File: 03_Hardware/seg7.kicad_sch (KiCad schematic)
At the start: 49 parts, among them Q201 BC807, U201 SMA41056

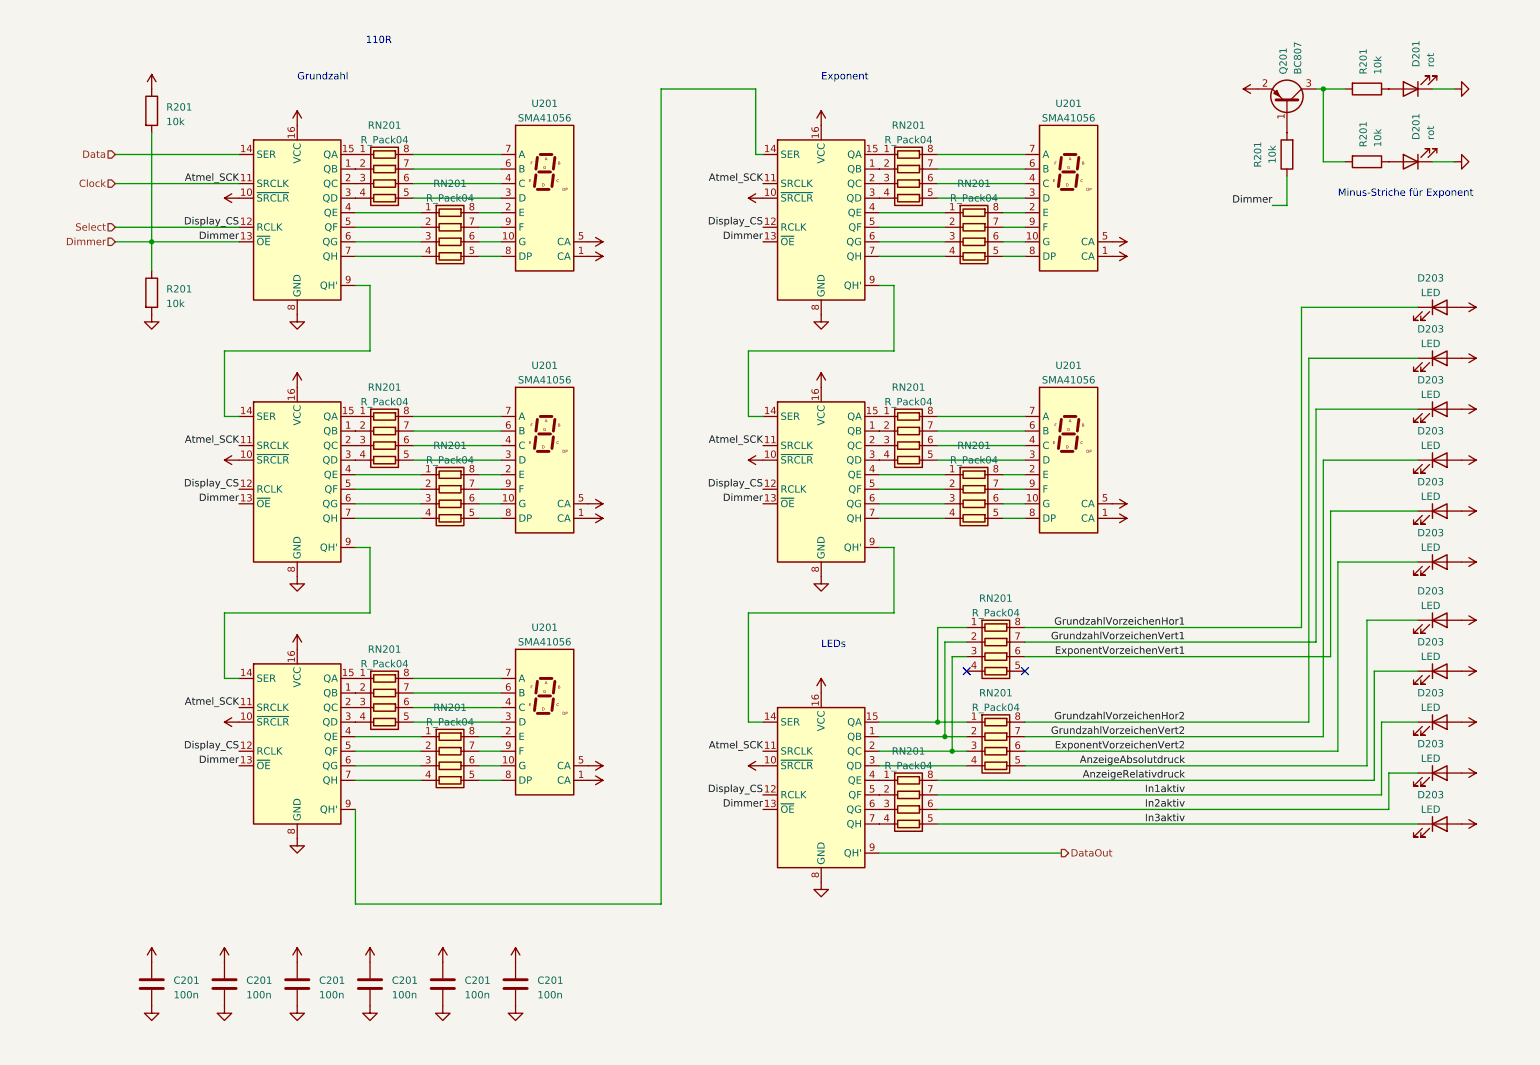
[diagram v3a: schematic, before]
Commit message: Anzeigen an bestellte Modelle angepasst
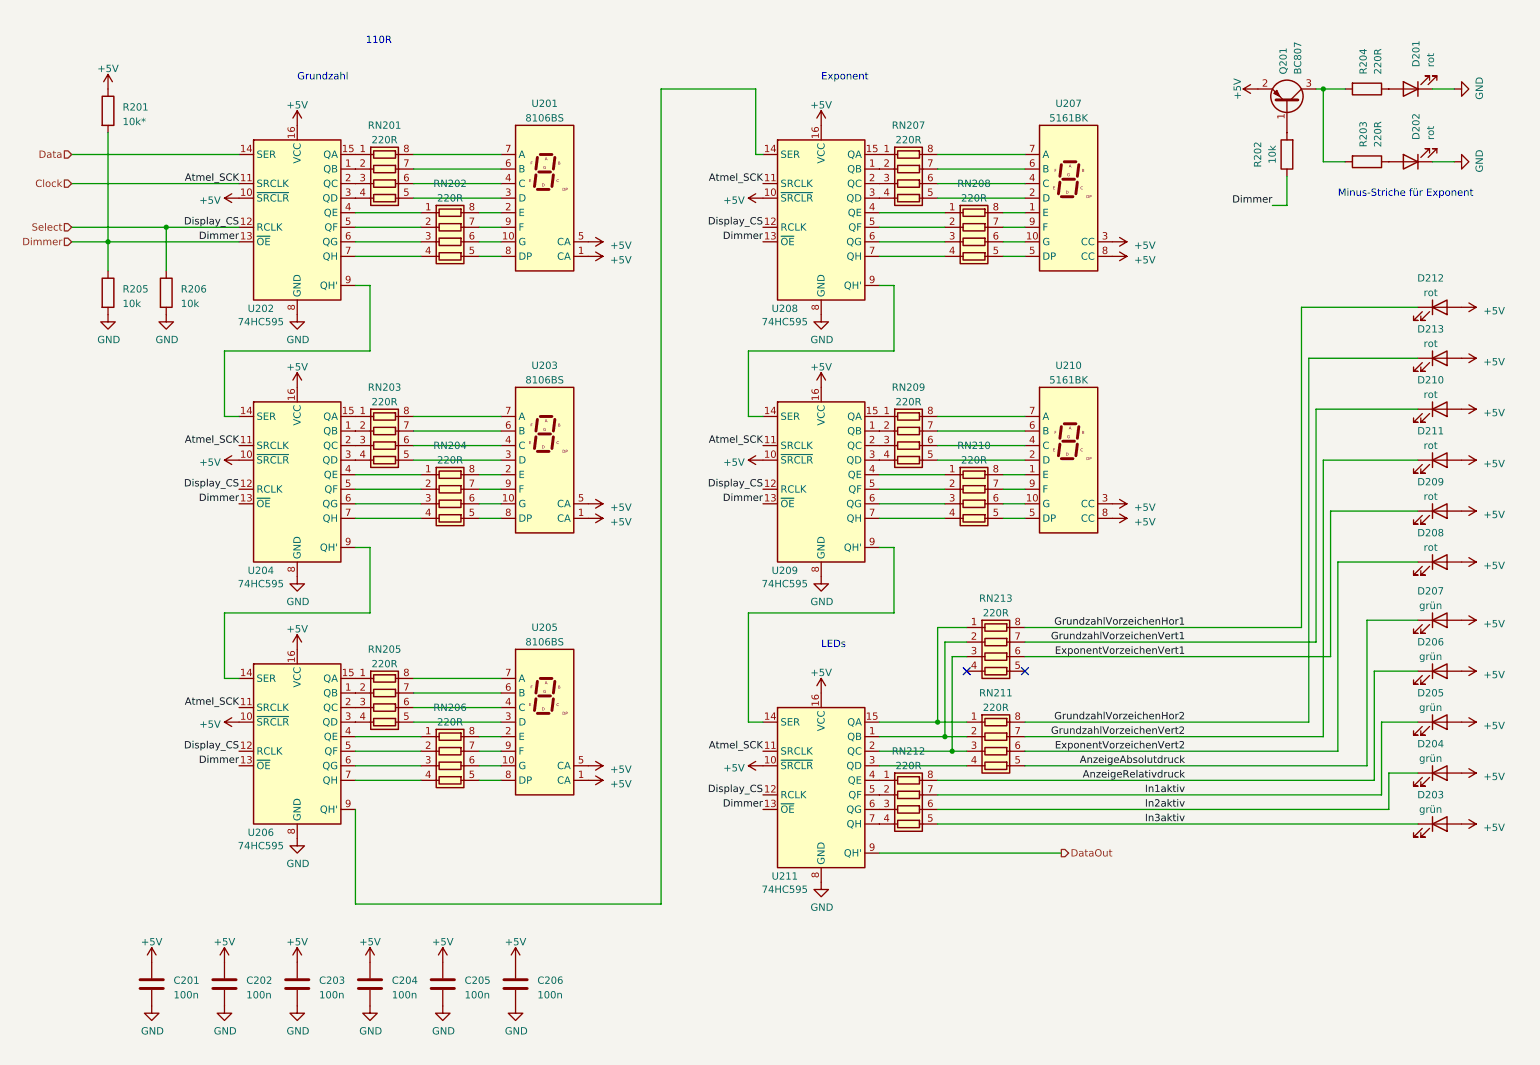
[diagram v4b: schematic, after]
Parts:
- removed U201 (x2): SMA41056, Display_7Segment:SA15-11xxx, symbol Display_Character:SA15-11EWA
- added R206: 10k, Resistor_SMD:R_0603_1608Metric, symbol Device:R
- added U207, U210: 5161BK, Display_7Segment:D1X8K, symbol Display_Character:D168K
- D201: footprint (none) -> LED_THT:LED_Rectangular_W3.0mm_H2.0mm
- D202: renamed from D201; footprint (none) -> LED_THT:LED_Rectangular_W3.0mm_H2.0mm
- D203: value LED -> grün; footprint (none) -> LED_THT:LED_D5.0mm
- D204, D205, D206, D207: renamed from D203; value LED -> grün; footprint (none) -> LED_THT:LED_D5.0mm
- D208, D209, D210, D211, D212, D213: renamed from D203; value LED -> rot; footprint (none) -> LED_THT:LED_Rectangular_W3.0mm_H2.0mm
- R201: value 10k -> 10k*; footprint (none) -> Resistor_SMD:R_0603_1608Metric
- R202, R205: renamed from R201; footprint (none) -> Resistor_SMD:R_0603_1608Metric
- R203, R204: renamed from R201; value 10k -> 220R; footprint (none) -> Resistor_SMD:R_0603_1608Metric
- RN201: value R_Pack04 -> 220R; footprint (none) -> Resistor_SMD:R_Array_Convex_4x1206
- RN202, RN203, RN204, RN205, RN206, RN207, RN208, RN209, RN210, RN211, RN212, RN213: renamed from RN201; value R_Pack04 -> 220R; footprint (none) -> Resistor_SMD:R_Array_Convex_4x1206
- U201: value SMA41056 -> 8106BS; footprint Display_7Segment:SA15-11xxx -> board:8106BS
- U202, U204, U206, U208, U209, U211: renamed from ?; value (none) -> 74HC595; footprint (none) -> Package_SO:SOIC-16_3.9x9.9mm_P1.27mm
- U203, U205: renamed from U201; value SMA41056 -> 8106BS; footprint Display_7Segment:SA15-11xxx -> board:8106BS
- renumbered C201 to C202, C201 to C203, C201 to C204, C201 to C205, C201 to C206
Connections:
- net +5V: now also U207.3 (CC), U207.8 (CC), U210.3 (CC), U210.8 (CC)
- net GND: now also R206.2
- net Select: now also R206.1
- net at RN210.5 (R4.2): now also U210.5 (DP)
- net at RN210.6 (R3.2): now also U210.10 (G)
- net at RN210.7 (R2.2): now also U210.9 (F)
- net at RN210.8 (R1.2): now also U210.1 (E)
- net at RN209.5 (R4.2): now also U210.2 (D)
- net at RN209.6 (R3.2): now also U210.4 (C)
- net at RN209.7 (R2.2): now also U210.6 (B)
- net at RN209.8 (R1.2): now also U210.7 (A)
- net at RN208.5 (R4.2): now also U207.5 (DP)
- net at RN208.6 (R3.2): now also U207.10 (G)
- net at RN208.7 (R2.2): now also U207.9 (F)
- net at RN208.8 (R1.2): now also U207.1 (E)
- net at RN207.5 (R4.2): now also U207.2 (D)
- net at RN207.6 (R3.2): now also U207.4 (C)
- net at RN207.7 (R2.2): now also U207.6 (B)
- net at RN207.8 (R1.2): now also U207.7 (A)
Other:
- moved on the sheet: R201, R205

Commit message: kleine änderungen
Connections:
- net at U201.10 (G): now also RN202.7 (R2.2); no longer RN202.6 (R3.2)
- net at U201.2 (E): now also RN202.5 (R4.2); no longer RN202.8 (R1.2)
- net at U201.3 (D): now also RN201.8 (R1.2); no longer RN201.5 (R4.2)
- net at U201.4 (C): now also RN201.7 (R2.2); no longer RN201.6 (R3.2)
- net at U201.6 (B): now also RN201.6 (R3.2); no longer RN201.7 (R2.2)
- net at U201.7 (A): now also RN201.5 (R4.2); no longer RN201.8 (R1.2)
- net at U201.8 (DP): now also RN202.8 (R1.2); no longer RN202.5 (R4.2)
- net at U201.9 (F): now also RN202.6 (R3.2); no longer RN202.7 (R2.2)
- net at U208.1 (QB): now also RN207.3 (R3.1); no longer RN207.2 (R2.1)
- net at U208.15 (QA): now also RN207.4 (R4.1); no longer RN207.1 (R1.1)
- net at U208.2 (QC): now also RN207.2 (R2.1); no longer RN207.3 (R3.1)
- net at U208.3 (QD): now also RN207.1 (R1.1); no longer RN207.4 (R4.1)
- net at U208.4 (QE): now also RN208.4 (R4.1); no longer RN208.1 (R1.1)
- net at U208.5 (QF): now also RN208.3 (R3.1); no longer RN208.2 (R2.1)
- net at U208.6 (QG): now also RN208.2 (R2.1); no longer RN208.3 (R3.1)
- net at U208.7 (QH): now also RN208.1 (R1.1); no longer RN208.4 (R4.1)
- net at U204.1 (QB): now also RN203.3 (R3.1); no longer RN203.2 (R2.1)
- net at U204.15 (QA): now also RN203.4 (R4.1); no longer RN203.1 (R1.1)
- net at U204.2 (QC): now also RN203.2 (R2.1); no longer RN203.3 (R3.1)
- net at U204.3 (QD): now also RN203.1 (R1.1); no longer RN203.4 (R4.1)
- net at U204.4 (QE): now also RN204.4 (R4.1); no longer RN204.1 (R1.1)
- net at U204.5 (QF): now also RN204.3 (R3.1); no longer RN204.2 (R2.1)
- net at U204.6 (QG): now also RN204.2 (R2.1); no longer RN204.3 (R3.1)
- net at U204.7 (QH): now also RN204.1 (R1.1); no longer RN204.4 (R4.1)
- net at RN202.1 (R1.1): now also U202.7 (QH); no longer U202.4 (QE)
- net at RN202.2 (R2.1): now also U202.6 (QG); no longer U202.5 (QF)
- net at RN202.3 (R3.1): now also U202.5 (QF); no longer U202.6 (QG)
- net at RN202.4 (R4.1): now also U202.4 (QE); no longer U202.7 (QH)
- net at U209.1 (QB): now also RN209.3 (R3.1); no longer RN209.2 (R2.1)
- net at U209.15 (QA): now also RN209.4 (R4.1); no longer RN209.1 (R1.1)
- net at U209.2 (QC): now also RN209.2 (R2.1); no longer RN209.3 (R3.1)
- net at U209.3 (QD): now also RN209.1 (R1.1); no longer RN209.4 (R4.1)
- net at U209.4 (QE): now also RN210.4 (R4.1); no longer RN210.1 (R1.1)
- net at U209.5 (QF): now also RN210.3 (R3.1); no longer RN210.2 (R2.1)
- net at U209.6 (QG): now also RN210.2 (R2.1); no longer RN210.3 (R3.1)
- net at U209.7 (QH): now also RN210.1 (R1.1); no longer RN210.4 (R4.1)
- net at RN205.1 (R1.1): now also U206.3 (QD); no longer U206.15 (QA)
- net at RN205.2 (R2.1): now also U206.2 (QC); no longer U206.1 (QB)
- net at RN205.3 (R3.1): now also U206.1 (QB); no longer U206.2 (QC)
- net at RN205.4 (R4.1): now also U206.15 (QA); no longer U206.3 (QD)
- net at RN205.5 (R4.2): now also U205.7 (A); no longer U205.3 (D)
- net at RN205.6 (R3.2): now also U205.6 (B); no longer U205.4 (C)
- net at RN205.7 (R2.2): now also U205.4 (C); no longer U205.6 (B)
- net at RN205.8 (R1.2): now also U205.3 (D); no longer U205.7 (A)
- net at U207.1 (E): now also RN208.5 (R4.2); no longer RN208.8 (R1.2)
- net at U207.10 (G): now also RN208.7 (R2.2); no longer RN208.6 (R3.2)
- net at U207.2 (D): now also RN207.8 (R1.2); no longer RN207.5 (R4.2)
- net at U207.4 (C): now also RN207.7 (R2.2); no longer RN207.6 (R3.2)
- net at U207.5 (DP): now also RN208.8 (R1.2); no longer RN208.5 (R4.2)
- net at U207.6 (B): now also RN207.6 (R3.2); no longer RN207.7 (R2.2)
- net at U207.7 (A): now also RN207.5 (R4.2); no longer RN207.8 (R1.2)
- net at U207.9 (F): now also RN208.6 (R3.2); no longer RN208.7 (R2.2)
- net at RN201.1 (R1.1): now also U202.3 (QD); no longer U202.15 (QA)
- net at RN201.2 (R2.1): now also U202.2 (QC); no longer U202.1 (QB)
- net at RN201.3 (R3.1): now also U202.1 (QB); no longer U202.2 (QC)
- net at RN201.4 (R4.1): now also U202.15 (QA); no longer U202.3 (QD)
- net at RN210.5 (R4.2): now also U210.1 (E); no longer U210.5 (DP)
- net at RN210.6 (R3.2): now also U210.9 (F); no longer U210.10 (G)
- net at RN210.7 (R2.2): now also U210.10 (G); no longer U210.9 (F)
- net at RN210.8 (R1.2): now also U210.5 (DP); no longer U210.1 (E)
- net at RN204.5 (R4.2): now also U203.2 (E); no longer U203.8 (DP)
- net at RN204.6 (R3.2): now also U203.9 (F); no longer U203.10 (G)
- net at RN204.7 (R2.2): now also U203.10 (G); no longer U203.9 (F)
- net at RN204.8 (R1.2): now also U203.8 (DP); no longer U203.2 (E)
- net at U205.10 (G): now also RN206.7 (R2.2); no longer RN206.6 (R3.2)
- net at U205.2 (E): now also RN206.5 (R4.2); no longer RN206.8 (R1.2)
- net at U205.8 (DP): now also RN206.8 (R1.2); no longer RN206.5 (R4.2)
- net at U205.9 (F): now also RN206.6 (R3.2); no longer RN206.7 (R2.2)
- net at U203.3 (D): now also RN203.8 (R1.2); no longer RN203.5 (R4.2)
- net at U203.4 (C): now also RN203.7 (R2.2); no longer RN203.6 (R3.2)
- net at U203.6 (B): now also RN203.6 (R3.2); no longer RN203.7 (R2.2)
- net at U203.7 (A): now also RN203.5 (R4.2); no longer RN203.8 (R1.2)
- net at U210.2 (D): now also RN209.8 (R1.2); no longer RN209.5 (R4.2)
- net at U210.4 (C): now also RN209.7 (R2.2); no longer RN209.6 (R3.2)
- net at U210.6 (B): now also RN209.6 (R3.2); no longer RN209.7 (R2.2)
- net at U210.7 (A): now also RN209.5 (R4.2); no longer RN209.8 (R1.2)
- net at RN206.1 (R1.1): now also U206.7 (QH); no longer U206.4 (QE)
- net at RN206.2 (R2.1): now also U206.6 (QG); no longer U206.5 (QF)
- net at RN206.3 (R3.1): now also U206.5 (QF); no longer U206.6 (QG)
- net at RN206.4 (R4.1): now also U206.4 (QE); no longer U206.7 (QH)

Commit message: Stecker fertig ausgewählt und Layout etwa 60% fertig
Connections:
- net AnzeigeRelativdruck: now also RN212.5 (R4.2); no longer RN212.8 (R1.2)
- net In1aktiv: now also RN212.6 (R3.2); no longer RN212.7 (R2.2)
- net In2aktiv: now also RN212.7 (R2.2); no longer RN212.6 (R3.2)
- net In3aktiv: now also RN212.8 (R1.2); no longer RN212.5 (R4.2)
- net at U201.10 (G): now also RN201.5 (R4.2); no longer RN202.7 (R2.2)
- net at U201.2 (E): now also RN202.8 (R1.2); no longer RN202.5 (R4.2)
- net at U201.3 (D): now also RN202.7 (R2.2); no longer RN201.8 (R1.2)
- net at U201.4 (C): now also RN202.6 (R3.2); no longer RN201.7 (R2.2)
- net at U201.6 (B): now also RN202.5 (R4.2); no longer RN201.6 (R3.2)
- net at U201.7 (A): now also RN201.8 (R1.2); no longer RN201.5 (R4.2)
- net at U201.8 (DP): now also RN201.7 (R2.2); no longer RN202.8 (R1.2)
- net at U201.9 (F): now also RN201.6 (R3.2); no longer RN202.6 (R3.2)
- net at RN212.1 (R1.1): now also U211.7 (QH); no longer U211.4 (QE)
- net at RN212.2 (R2.1): now also U211.6 (QG); no longer U211.5 (QF)
- net at RN212.3 (R3.1): now also U211.5 (QF); no longer U211.6 (QG)
- net at RN212.4 (R4.1): now also U211.4 (QE); no longer U211.7 (QH)
- net at RN205.5 (R4.2): now also U205.10 (G); no longer U205.7 (A)
- net at RN205.6 (R3.2): now also U205.9 (F); no longer U205.6 (B)
- net at RN205.7 (R2.2): now also U205.8 (DP); no longer U205.4 (C)
- net at RN205.8 (R1.2): now also U205.7 (A); no longer U205.3 (D)
- net at RN204.5 (R4.2): now also U203.6 (B); no longer U203.2 (E)
- net at RN204.6 (R3.2): now also U203.4 (C); no longer U203.9 (F)
- net at RN204.7 (R2.2): now also U203.3 (D); no longer U203.10 (G)
- net at RN204.8 (R1.2): now also U203.2 (E); no longer U203.8 (DP)
- net at RN206.7 (R2.2): now also U205.3 (D); no longer U205.10 (G)
- net at U205.2 (E): now also RN206.8 (R1.2); no longer RN206.5 (R4.2)
- net at RN206.6 (R3.2): now also U205.4 (C); no longer U205.9 (F)
- net at RN203.8 (R1.2): now also U203.7 (A); no longer U203.3 (D)
- net at RN203.7 (R2.2): now also U203.8 (DP); no longer U203.4 (C)
- net at RN203.6 (R3.2): now also U203.9 (F); no longer U203.6 (B)
- net at RN203.5 (R4.2): now also U203.10 (G); no longer U203.7 (A)
- new net: RN206.5 (R4.2), U205.6 (B)
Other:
- moved on the sheet: RN202, RN204, RN206, U201, U203, U205

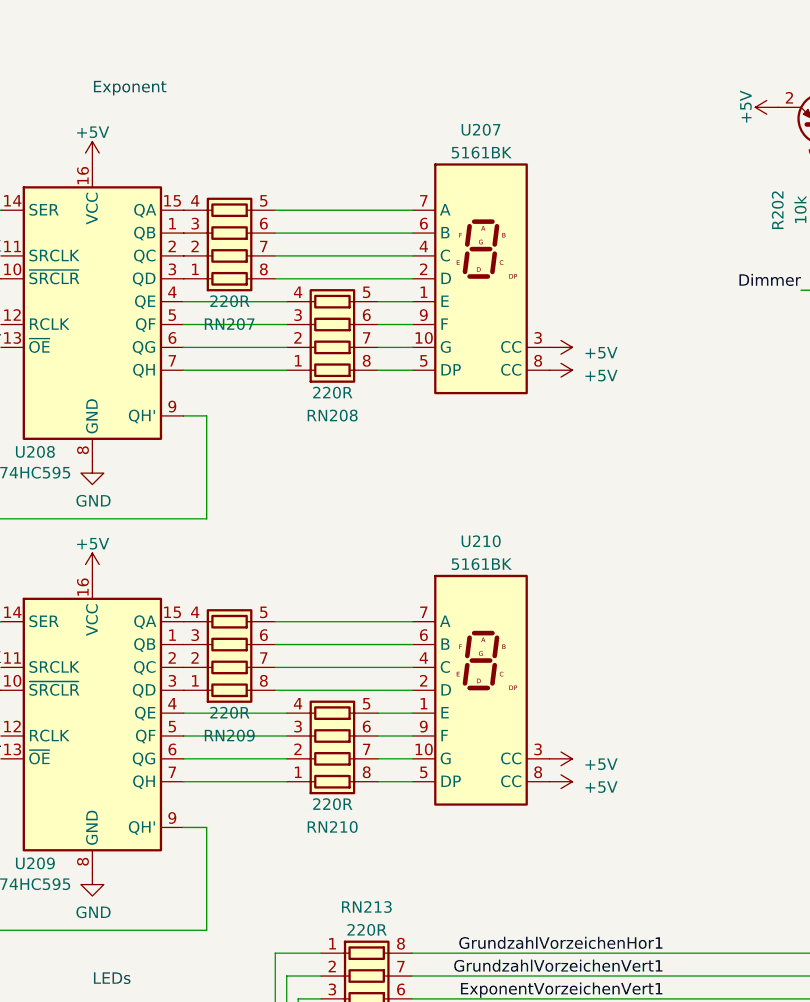
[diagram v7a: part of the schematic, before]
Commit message: Layout aktuell fast DRC-Fehlerfrei, Überlappungen von Plus-Zeichen sind in Ordnung. Texte müssen noch ausgerichtet werden!
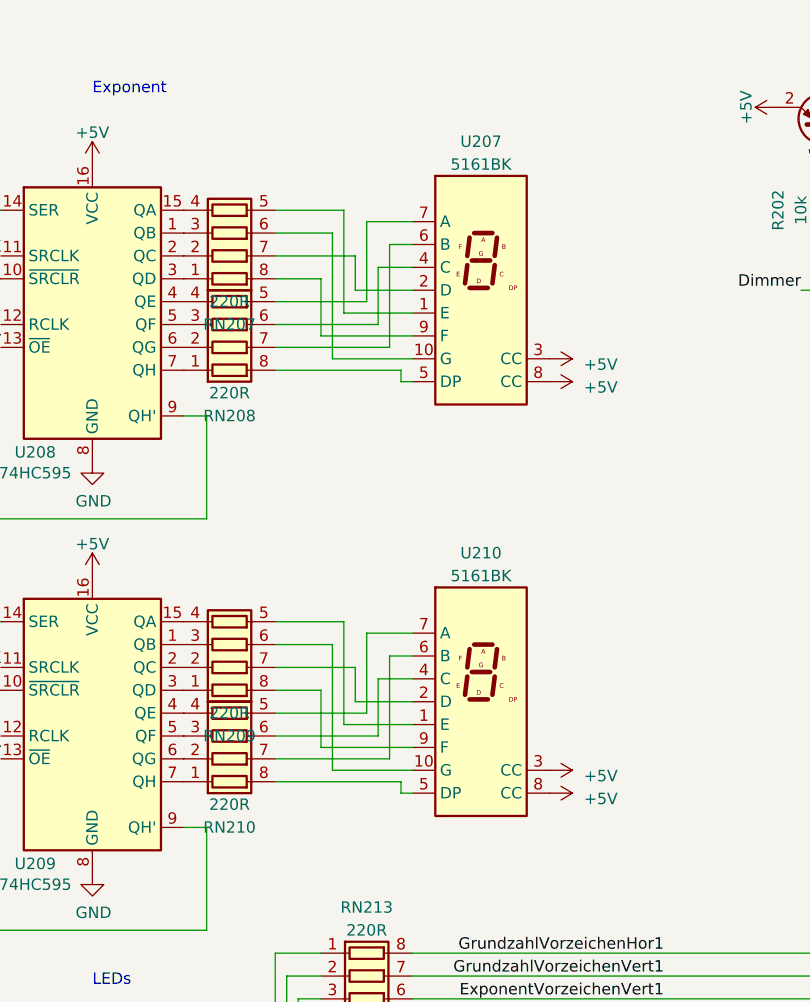
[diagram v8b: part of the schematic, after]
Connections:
- net at U207.1 (E): now also RN207.5 (R4.2); no longer RN208.5 (R4.2)
- net at U207.10 (G): now also RN207.6 (R3.2); no longer RN208.7 (R2.2)
- net at U207.2 (D): now also RN207.7 (R2.2); no longer RN207.8 (R1.2)
- net at U207.4 (C): now also RN208.6 (R3.2); no longer RN207.7 (R2.2)
- net at U207.6 (B): now also RN208.7 (R2.2); no longer RN207.6 (R3.2)
- net at U207.7 (A): now also RN208.5 (R4.2); no longer RN207.5 (R4.2)
- net at U207.9 (F): now also RN207.8 (R1.2); no longer RN208.6 (R3.2)
- net at RN210.5 (R4.2): now also U210.7 (A); no longer U210.1 (E)
- net at RN210.6 (R3.2): now also U210.4 (C); no longer U210.9 (F)
- net at RN210.7 (R2.2): now also U210.6 (B); no longer U210.10 (G)
- net at U210.2 (D): now also RN209.7 (R2.2); no longer RN209.8 (R1.2)
- net at RN209.6 (R3.2): now also U210.10 (G); no longer U210.6 (B)
- net at RN209.5 (R4.2): now also U210.1 (E); no longer U210.7 (A)
- new net: RN209.8 (R1.2), U210.9 (F)
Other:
- moved on the sheet: RN208, RN210, U207, U210
